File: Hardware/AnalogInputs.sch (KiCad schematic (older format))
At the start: 16 parts, among them J2 Screw_Terminal_01x03, J3 Screw_Terminal_01x03, U7 MCP6001-OT, U8 MCP6001-OT

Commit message: PCB router 50%
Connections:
- net 3V3_POT1: now also D11.1 (A1), U7.5 (V+)
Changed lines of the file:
@@
 EESchema Schematic File Version 4
-EELAYER 30 0
+LIBS:APPS-cache
+EELAYER 29 0
 EELAYER END
 $Descr A4 11693 8268
@@
 Text GLabel 2750 1550 1    50   Input ~ 0
 3V3_POT1
-Text GLabel 3550 1700 1    50   Input ~ 0
+Text GLabel 3550 1750 1    50   Input ~ 0
 3V3_POT1
-Text GLabel 4150 1850 1    50   Input ~ 0
+Text GLabel 4150 1900 1    50   Input ~ 0
 3V3_POT1
 Text GLabel 2750 3250 1    50   Input ~ 0

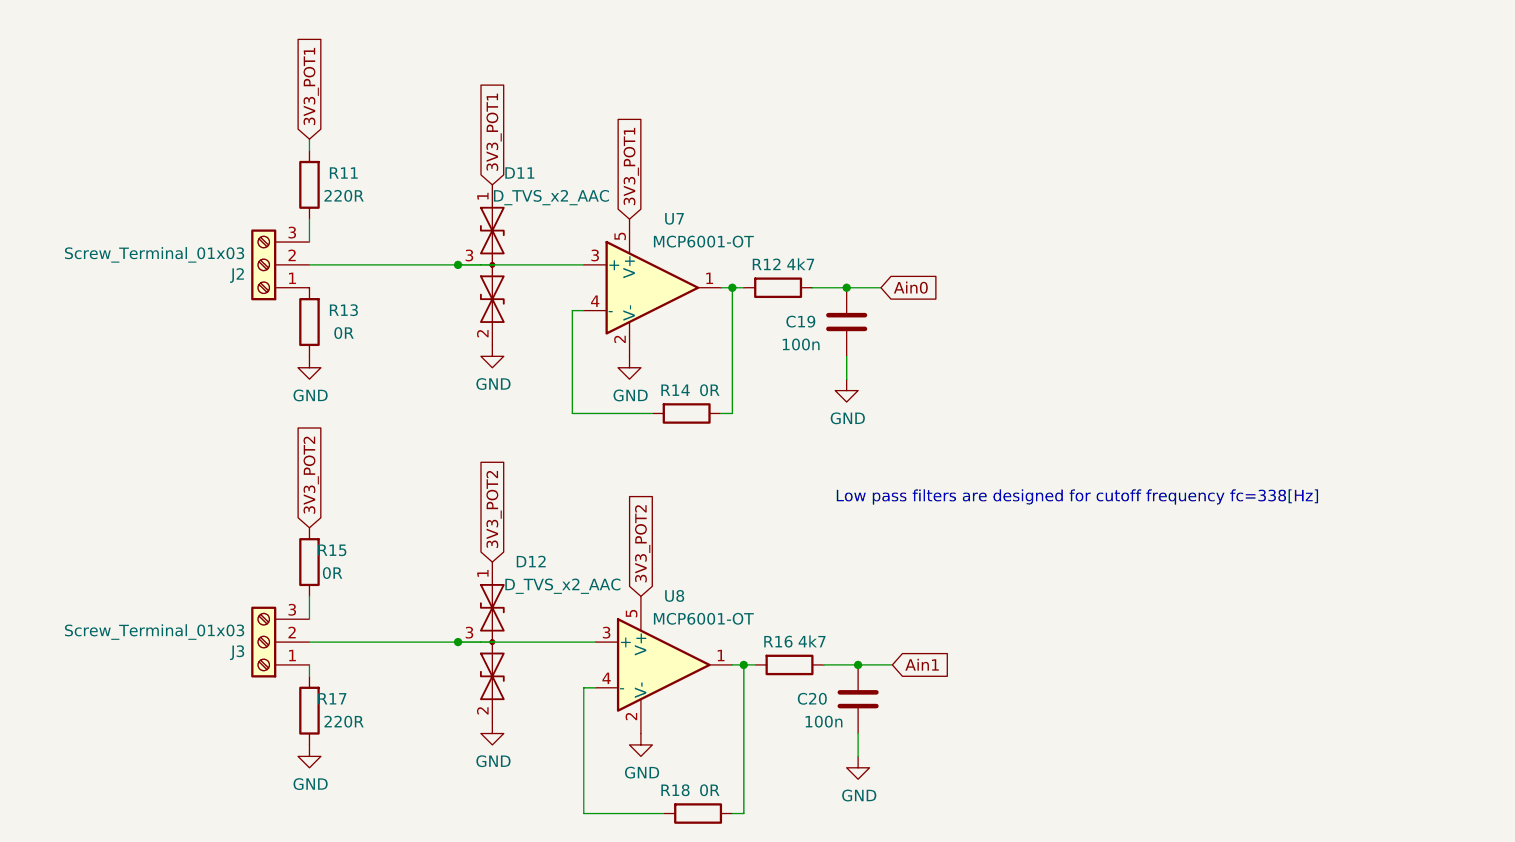
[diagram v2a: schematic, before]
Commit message: Components labels placed
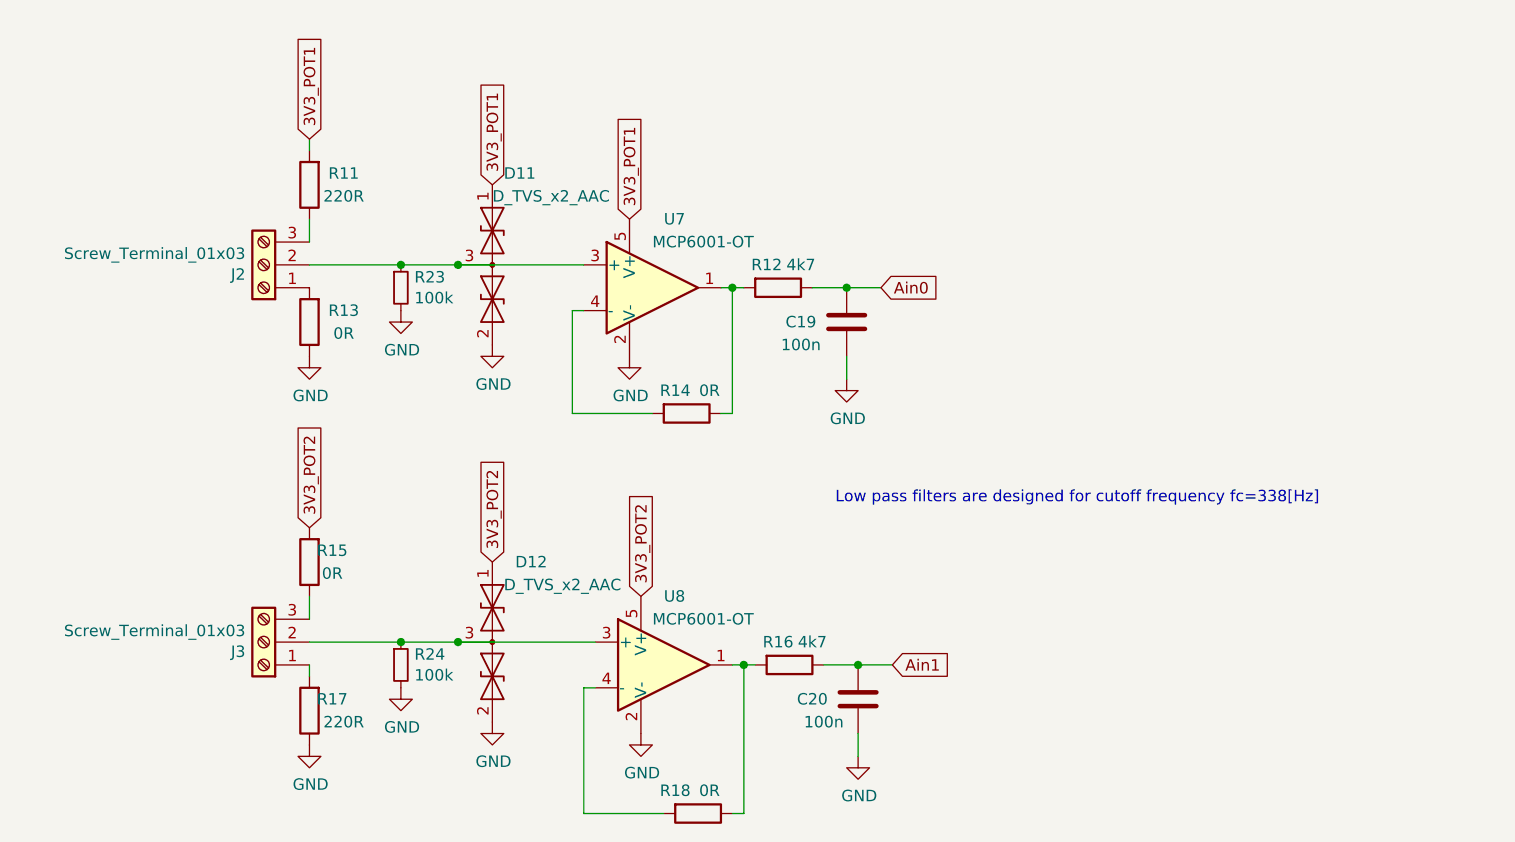
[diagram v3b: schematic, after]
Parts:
- added R23, R24: 100k, Resistor_SMD:R_1206_3216Metric, symbol Device:R_Small
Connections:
- net GND: now also R23.2, R24.2
- net at D12.3 (common), J3.2 (Pin_2), U8.3 (+): now also R24.1
- net at D11.3 (common), J2.2 (Pin_2), U7.3 (+): now also R23.1
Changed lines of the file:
@@
 	4000 3750 3400 3750
 Wire Wire Line
-	3400 3750 2750 3750
+	3400 3750 3150 3750
 Connection ~ 3400 3750
 $Comp
@@
 	3950 2100 3400 2100
 Wire Wire Line
-	3400 2100 2750 2100
+	3400 2100 3150 2100
 Connection ~ 3400 2100
 Text GLabel 2750 1550 1    50   Input ~ 0
@@
 Wire Wire Line
 	2750 1550 2750 1600
+$Comp
+L Device:R_Small R23
+U 1 1 60AC6F3F
+P 3150 2200
+F 0 "R23" H 3209 2246 50  0000 L CNN
+F 1 "100k" H 3209 2155 50  0000 L CNN
+F 2 "Resistor_SMD:R_1206_3216Metric" H 3150 2200 50  0001 C CNN
+F 3 "~" H 3150 2200 50  0001 C CNN
+	1    3150 2200
+	1    0    0    -1
+$EndComp
+Connection ~ 3150 2100
+Wire Wire Line
+	3150 2100 2750 2100
+$Comp
+L power:GND #PWR0102
+U 1 1 60AC767D
+P 3150 2300
+F 0 "#PWR0102" H 3150 2050 50  0001 C CNN
+F 1 "GND" H 3155 2127 50  0000 C CNN
+F 2 "" H 3150 2300 50  0001 C CNN
+F 3 "" H 3150 2300 50  0001 C CNN
+	1    3150 2300
+	1    0    0    -1
+$EndComp
+$Comp
+L Device:R_Small R24
+U 1 1 60AC7E5A
+P 3150 3850
+F 0 "R24" H 3209 3896 50  0000 L CNN
+F 1 "100k" H 3209 3805 50  0000 L CNN
+F 2 "Resistor_SMD:R_1206_3216Metric" H 3150 3850 50  0001 C CNN
+F 3 "~" H 3150 3850 50  0001 C CNN
+	1    3150 3850
+	1    0    0    -1
+$EndComp
+$Comp
+L power:GND #PWR0103
+U 1 1 60AC7E60
+P 3150 3950
+F 0 "#PWR0103" H 3150 3700 50  0001 C CNN
+F 1 "GND" H 3155 3777 50  0000 C CNN
+F 2 "" H 3150 3950 50  0001 C CNN
+F 3 "" H 3150 3950 50  0001 C CNN
+	1    3150 3950
+	1    0    0    -1
+$EndComp
+Connection ~ 3150 3750
+Wire Wire Line
+	3150 3750 2750 3750
 $EndSCHEMATC
